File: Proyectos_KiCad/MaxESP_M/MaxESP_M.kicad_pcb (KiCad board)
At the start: 2 copper layers, 74 x 100 mm, 62 parts, among them J1 DC, J10 RJ45, J11 RJ45, J12 RJ45, J13 RJ45, J14 VOL SEL, J2 ON/OFF, J3 PJ-325M/3.5MM, J4 DA15, J5 Conn_01x04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

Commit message: Por si valgo
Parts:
- removed J4: DA15, Connector_Dsub:DSUB-15_Pins_Horizontal_P2.77x2.84mm_EdgePinOffset4.94mm_Housed_MountingHolesOffset4.94mm
- C10, C11, C12, C2, C3, C4, C5, C7, C8: footprint PCM_Capacitor_SMD_Handsoldering_AKL:C_1206_3216Metric_Pad1.33x1.80mm -> PCM_Capacitor_SMD_Handsoldering_AKL:C_0805_2012Metric_Pad1.18x1.45mm
- C6, C9: footprint PCM_Capacitor_SMD_Handsoldering_AKL:C_1206_3216Metric_Pad1.33x1.80mm -> PCM_Capacitor_SMD_Handsoldering_AKL:C_0805_2012Metric_Pad1.18x1.45mm; moved to B.Cu
- D1, D6: moved to B.Cu
- D3, D4: footprint PCM_LED_SMD_Handsoldering_AKL:LED_1206_3216Metric_Pad1.42x1.75mm -> PCM_LED_SMD_AKL:LED_0805_2012Metric_Pad1.15x1.40mm
- J3: footprint Connector_Audio:Jack_3.5mm_CUI_SJ1-3535NG_Horizontal -> @EmersonPrez15:Jack_3.5mm_CUI_SJ1-3535NG_Horizontal
- R1, R2, R3, R4, R5, R6, R7: footprint PCM_Resistor_SMD_AKL:R_1206_3216Metric_Pad1.30x1.75mm -> PCM_Resistor_SMD_AKL:R_0805_2012Metric_Pad1.20x1.40mm_HandSolder; moved to B.Cu
- R10, R11, R12, R13, R14, R15, R16, R8, R9: footprint PCM_Resistor_SMD_AKL:R_1206_3216Metric_Pad1.30x1.75mm -> PCM_Resistor_SMD_AKL:R_0805_2012Metric_Pad1.20x1.40mm_HandSolder
- moved J8 147.4 mm to (120.9, 127.5), turned to 90 degrees
- moved D2 112.2 mm to (92.7, 112.5), turned to 90 degrees
- moved D1 108.1 mm to (124.0, 144.3)
- moved R3 103.1 mm to (116.8, 144.0), turned to -90 degrees
- moved R15 93.1 mm to (97.8, 66.0), turned to 180 degrees
- moved R1 87.2 mm to (124.0, 121.4), turned to -90 degrees
- moved R2 86.8 mm to (121.4, 121.4), turned to 90 degrees
- moved R8 83.8 mm to (119.6, 121.2), turned to 90 degrees
- moved D5 83.4 mm to (124.2, 115.6)
- moved C12 80.6 mm to (110.5, 61.0), turned to 180 degrees
- moved R9 79.9 mm to (121.9, 121.2), turned to 90 degrees
- moved D6 79.9 mm to (124.2, 112.8)
- moved C11 76.1 mm to (110.5, 68.6), turned to 180 degrees
- moved C6 76.1 mm to (109.2, 98.8), turned to 180 degrees
- moved R10 76.1 mm to (124.2, 121.2), turned to 90 degrees
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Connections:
- C10 pad 1: /Misc/PEC -> /ESP32S/PEC
- C11 pad 1: /Misc/AUX3 -> /ESP32S/AUX3
- C12 pad 1: /Misc/AUX4 -> /ESP32S/AUX4
- D4 pad 2: /Misc/STA -> /ESP32S/STA
- J5 pad 3: /Misc/AUX7 -> /ESP32S/AUX7
- J6 pad 3: /Misc/RA- -> /ESP32S/RA-
- J6 pad 4: /Misc/DE- -> /ESP32S/DE-
- J6 pad 5: /Misc/DE+ -> /ESP32S/DE+
- J6 pad 6: /Misc/RA+ -> /ESP32S/RA+
- J9 pad 3: /Misc/SCL -> /ESP32S/SCL
- J9 pad 4: /Misc/SDA -> /ESP32S/SDA
- R2 pad 2: /Misc/AUX8 -> /ESP32S/AUX8
- R3 pad 2: /Misc/STA -> /ESP32S/STA
- R4 pad 2: /Misc/RA+ -> /ESP32S/RA+
- R5 pad 2: /Misc/DE+ -> /ESP32S/DE+
- R6 pad 2: /Misc/DE- -> /ESP32S/DE-
- R7 pad 2: /Misc/RA- -> /ESP32S/RA-
- U1 pad 10: /ESP32S/DIR2 -> /Drivers/DIR2
- U1 pad 11: /ESP32S/STP2 -> /Drivers/STP2
- U1 pad 23: /ESP32S/DIR34 -> /Drivers/DIR34
- U1 pad 24: /ESP32S/SPT3 -> /Drivers/STP3
- U1 pad 25: /ESP32S/DIR1 -> /Drivers/DIR1
- U1 pad 26: /ESP32S/TXTMC -> /Drivers/TXTMC
- U1 pad 29: /ESP32S/EN -> /Drivers/EN
- U1 pad 30: /ESP32S/STP1 -> /Drivers/STP1
- U1 pad 31: /ESP32S/STP4 -> /Drivers/STP4
- U1 pad 4: /ESP32S/RXTMC -> /Drivers/RXTMC
- U4 pad 12: /Misc/TX2 -> /ESP32S/TX2
- U4 pad 13: /Misc/RX2 -> /ESP32S/RX2
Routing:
- net +3.3V: track 0.00 -> 393.9 mm, vias 0 -> 8
- net +5V: track 0.00 -> 205.5 mm, vias 0 -> 9
- net /ESP32S/STA: track 0.00 -> 158.0 mm
- net +12M: track 0.00 -> 143.3 mm, vias 0 -> 5
- net /Drivers/EN: track 0.00 -> 133.6 mm, vias 0 -> 4
- net /Drivers/DIR34: track 0.00 -> 124.8 mm, vias 0 -> 1
- net /Drivers/RXTMC: track 0.00 -> 119.4 mm, vias 0 -> 7
- net /Drivers/STP4: track 0.00 -> 117.4 mm
- net /ESP32S/AUX8: track 0.00 -> 111.4 mm, vias 0 -> 1
- net /ESP32S/RA-: track 0.00 -> 110.2 mm, vias 0 -> 1
- net /ESP32S/DE-: track 0.00 -> 103.3 mm, vias 0 -> 4
- net /Drivers/STP3: track 0.00 -> 102.9 mm
- net /ESP32S/RA+: track 0.00 -> 101.3 mm, vias 0 -> 1
- net /ESP32S/DE+: track 0.00 -> 92.8 mm, vias 0 -> 2
- net +12M2: track 0.00 -> 80.1 mm, vias 0 -> 3
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- added copper zone on B.Cu, net GND
- added copper zone on F.Cu, net GND

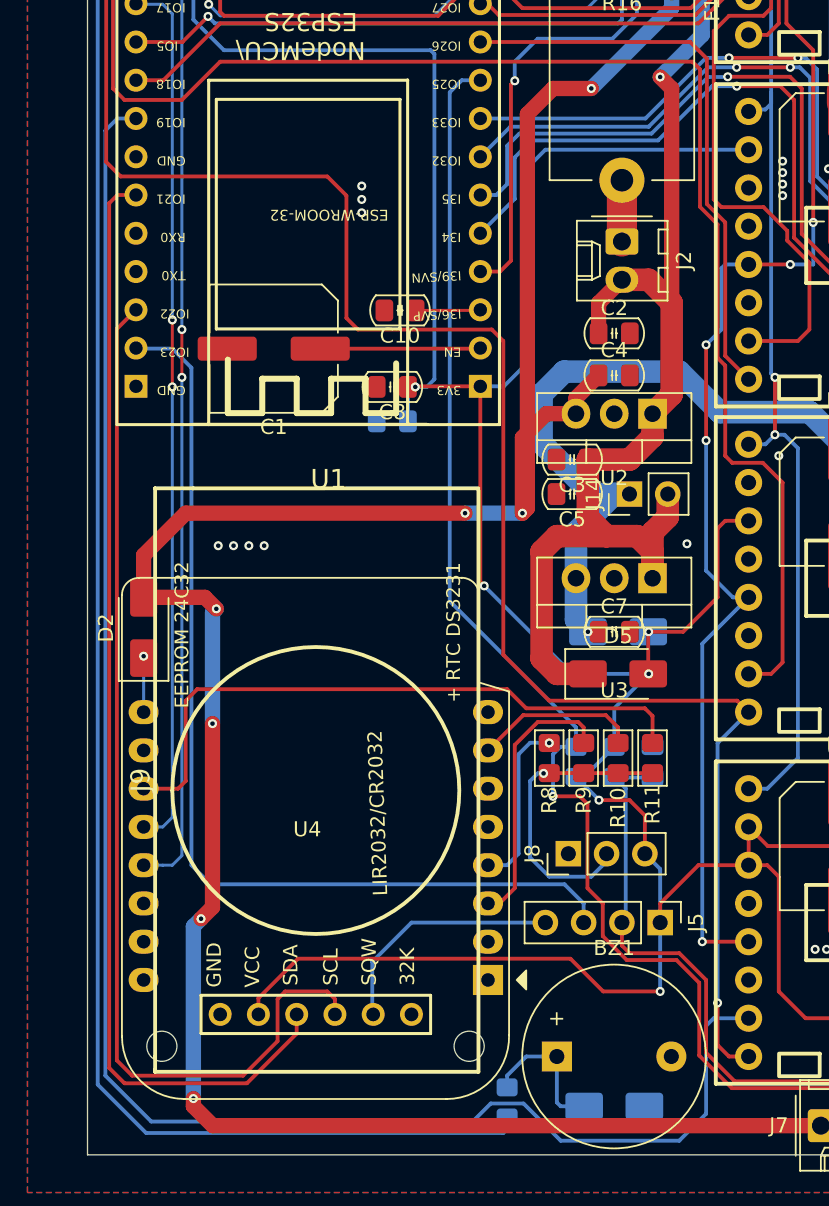
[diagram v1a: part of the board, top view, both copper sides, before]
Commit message: Moviendo el RTC y el WEMOS
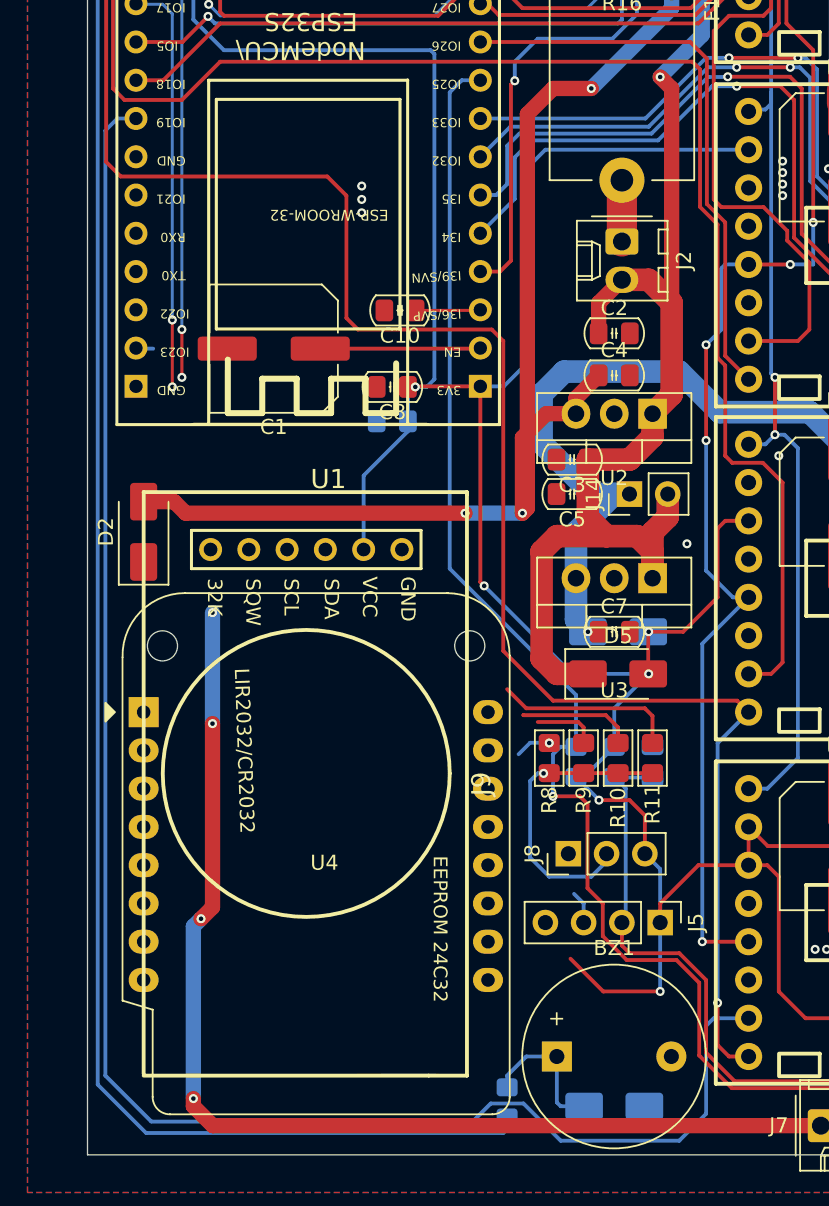
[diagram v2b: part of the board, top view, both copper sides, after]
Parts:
- moved J9 33.6 mm to (97.2, 107.3), turned to -90 degrees
- moved U4 29.0 mm to (92.7, 118.1), turned to 0 degrees
- moved D2 6.38 mm to (92.7, 106.1)
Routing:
- net /ESP32S/SDA: track 74.9 -> 0.00 mm
- net /ESP32S/SCL: track 70.4 -> 0.00 mm
- net /ESP32S/AUX7: track 65.7 -> 3.44 mm
- net /ESP32S/RX2: track 64.3 -> 29.7 mm
- net /ESP32S/TX2: track 58.3 -> 27.6 mm
- net /Misc/EN1_B: track 42.2 -> 12.9 mm
- net /Misc/PPS: track 16.7 -> 0.66 mm
- net /Misc/EN2_B: track 18.2 -> 4.33 mm
- net +3.3V: track 393.9 -> 380.7 mm
- net +5V: track 205.5 -> 196.3 mm
- net /Misc/EN2_A: track 11.8 -> 2.86 mm
- net unconnected-(U4-EN-Pad1): track 0.00 -> 3.72 mm
- net Net-(D2-K): track 3.72 -> 0.00 mm, vias 1 -> 0
- net /Misc/EN1_A: track 11.0 -> 7.66 mm
- net GND: vias 64 -> 61

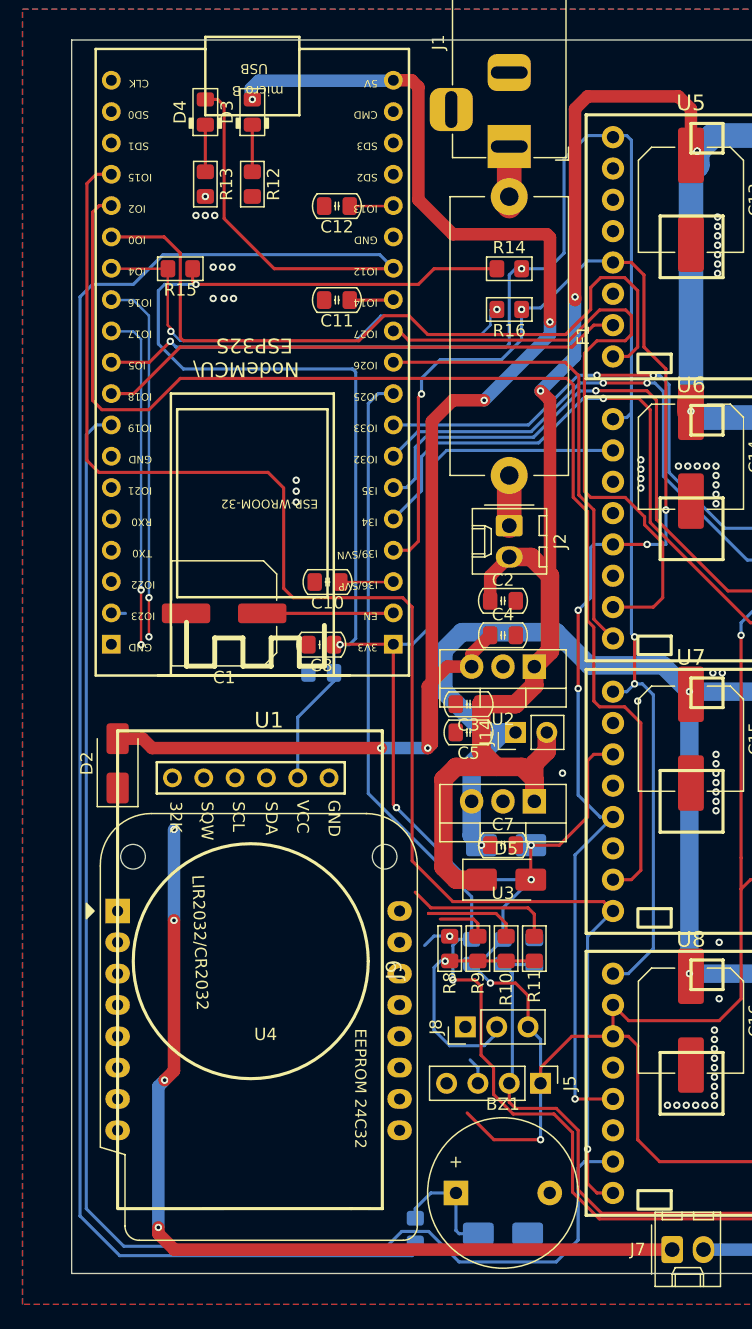
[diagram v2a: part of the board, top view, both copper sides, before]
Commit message: Arreglando RAM
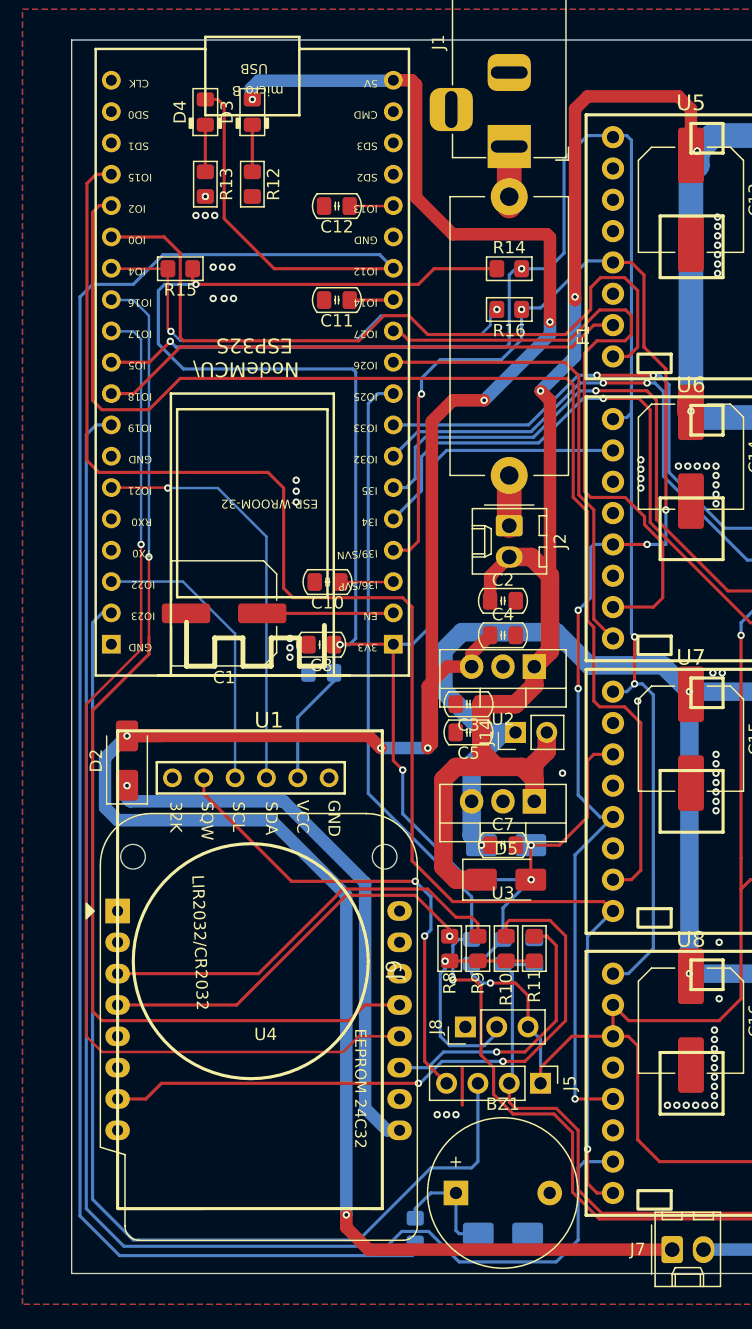
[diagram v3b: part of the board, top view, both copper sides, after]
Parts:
- moved D2 0.79 mm to (93.5, 105.9)
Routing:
- net /ESP32S/AUX7: track 3.44 -> 90.2 mm
- net /ESP32S/TX2: track 27.6 -> 87.6 mm, vias 2 -> 1
- net /ESP32S/RX2: track 29.7 -> 87.7 mm, vias 2 -> 1
- net Net-(D2-K): track 0.00 -> 45.0 mm, vias 0 -> 1
- net /Misc/EN1_A: track 7.66 -> 52.3 mm, vias 0 -> 2
- net /Misc/PPS: track 0.66 -> 40.1 mm, vias 0 -> 2
- net /ESP32S/SDA: track 0.00 -> 33.8 mm, vias 0 -> 1
- net /Misc/EN2_A: track 2.86 -> 32.8 mm
- net /Misc/EN2_B: track 4.33 -> 34.2 mm
- net /ESP32S/SCL: track 0.00 -> 23.5 mm
- net +3.3V: track 380.7 -> 369.8 mm, vias 8 -> 7
- net /Misc/EN1_B: track 12.9 -> 23.2 mm, vias 0 -> 1
- net +5V: track 196.3 -> 206.1 mm, vias 9 -> 7
- net unconnected-(U4-EN-Pad1): track 3.72 -> 0.00 mm
- net GND: track 0.00 -> 3.05 mm, vias 61 -> 66
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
